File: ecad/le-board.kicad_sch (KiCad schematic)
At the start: 72 parts

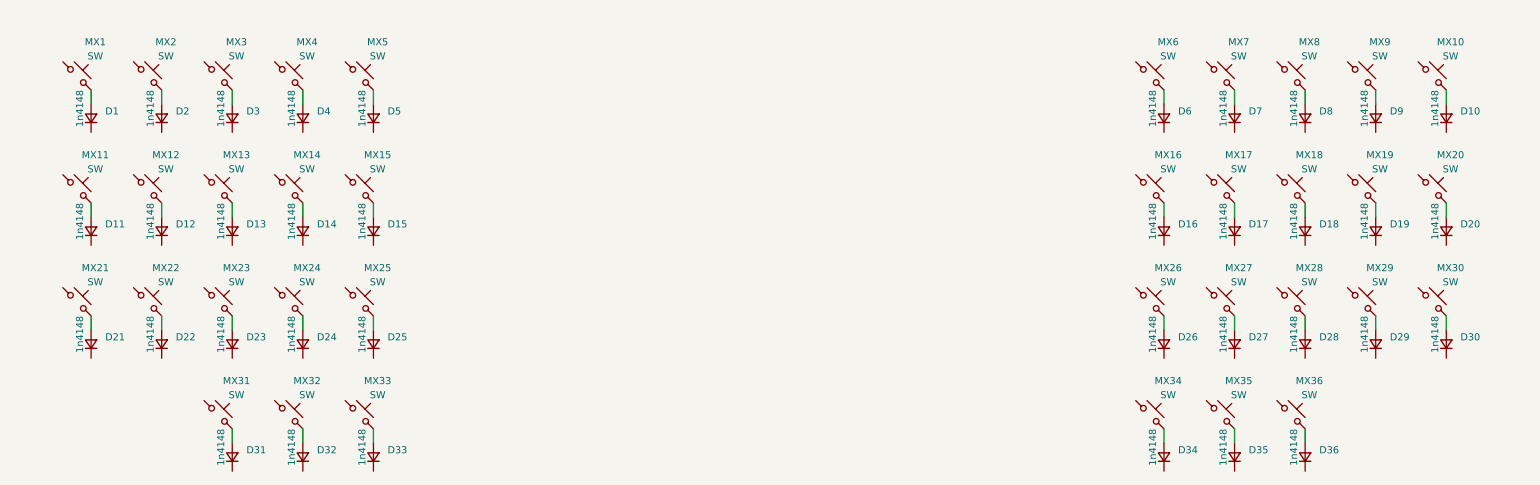
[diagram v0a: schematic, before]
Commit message: Added keyboard_pad_left, keyboard_pad_right. Added LDOs, Added USB C connector. Added initial placement for keys.
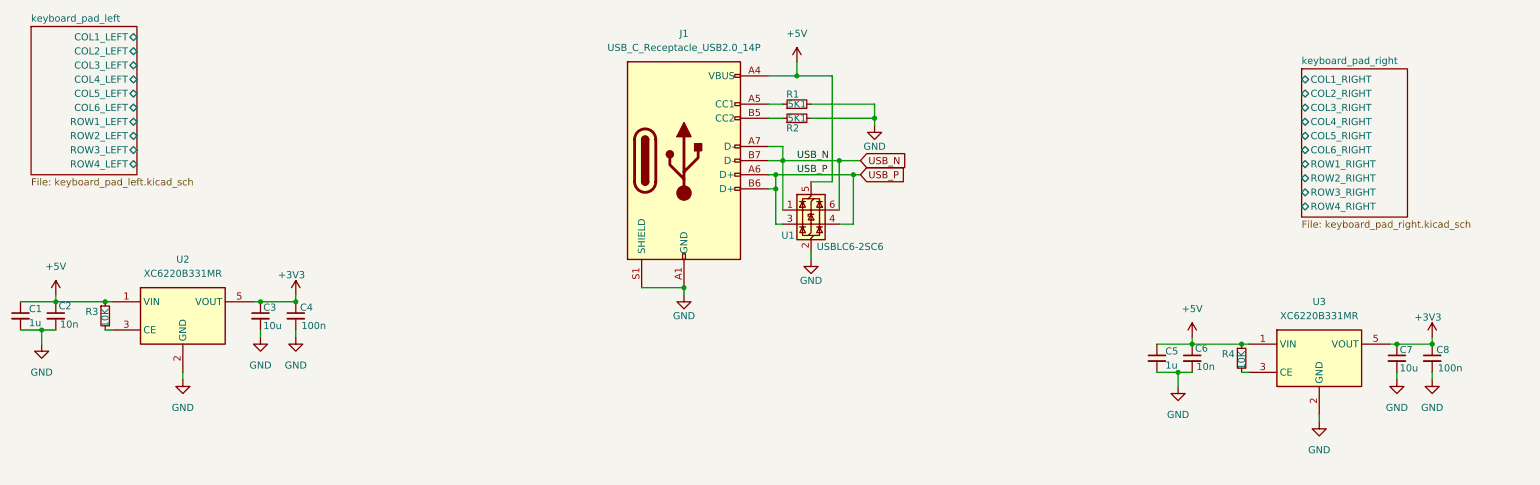
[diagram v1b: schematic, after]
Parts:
- removed D1, D10, D11, D12, D13, D14, D15, D16, D17, D18, D19, D2, D20, D21, D22, D23, D24, D25, D26, D27, D28, D29, D3, D30, D31, D32, D33, D34, D35, D36, D4, D5, D6, D7, D8, D9: 1n4148, Diode_SMD:D_SOD-123, symbol Device:D_Small
- removed MX1, MX10, MX11, MX12, MX13, MX14, MX15, MX16, MX17, MX18, MX19, MX2, MX20, MX21, MX22, MX23, MX24, MX25, MX26, MX27, MX28, MX29, MX3, MX30, MX31, MX32, MX33, MX34, MX35, MX36, MX4, MX5, MX6, MX7, MX8, MX9: SW, PCM_Switch_Keyboard_Cherry_MX:SW_Cherry_MX_PCB_1.00u, symbol PCM_marbastlib-mx:MX_SW_solder
- added C1, C5: 1u, Capacitor_SMD:C_0603_1608Metric, symbol Device:C_Small
- added C2, C6: 10n, Capacitor_SMD:C_0603_1608Metric, symbol Device:C_Small
- added C3, C7: 10u, Capacitor_SMD:C_0603_1608Metric, symbol Device:C_Small
- added C4, C8: 100n, Capacitor_SMD:C_0603_1608Metric, symbol Device:C_Small
- added J1: USB_C_Receptacle_USB2.0_14P, Connector_USB:USB_C_Receptacle_GCT_USB4105-xx-A_16P_TopMnt_Horizontal, symbol Connector:USB_C_Receptacle_USB2.0_14P
- added R1, R2: 5K1, Resistor_SMD:R_0402_1005Metric, symbol Device:R_Small
- added R3, R4: 10K, Resistor_SMD:R_0402_1005Metric, symbol Device:R_Small
- added U1: USBLC6-2SC6, Package_TO_SOT_SMD:SOT-23-6, symbol Power_Protection:USBLC6-2SC6
- added U2, U3: XC6220B331MR, Package_TO_SOT_SMD:SOT-23-5, symbol Regulator_Linear:XC6220B331MR
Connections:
- new net: J1.B5 (CC2), R2.1
- new net: R3.2, U2.3 (CE)
- new net: R4.2, U3.3 (CE)
- new net: J1.A5 (CC1), R1.1
- new net +3V3: C3.1, C4.1, C7.1, C8.1, U2.5 (VOUT), U3.5 (VOUT)
- new net +5V: C1.1, C2.1, C5.1, C6.1, J1.A4 (VBUS), J1.A9 (VBUS), J1.B4 (VBUS), J1.B9 (VBUS), R3.1, R4.1, U1.5 (VBUS), U2.1 (VIN), U3.1 (VIN)
- new net GND: C1.2, C2.2, C3.2, C4.2, C5.2, C6.2, C7.2, C8.2, J1.A1 (GND), J1.A12 (GND), J1.B1 (GND), J1.B12 (GND), J1.S1 (SHIELD), R1.2, R2.2, U1.2 (GND), U2.2 (GND), U3.2 (GND)
- new net USB_N: J1.A7 (D-), J1.B7 (D-), U1.1 (I/O1), U1.6 (I/O1)
- new net USB_P: J1.A6 (D+), J1.B6 (D+), U1.3 (I/O2), U1.4 (I/O2)
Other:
- added sheet keyboard_pad_left (keyboard_pad_left.kicad_sch)
- added sheet keyboard_pad_right (keyboard_pad_right.kicad_sch)

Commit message: Added 80% Schematic Finished.
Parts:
- added C10, C11, C21, C22: 100pF, symbol Device:C_Small
- added C12, C13, C19, C20: 1uF, symbol Device:C_Small
- added C14, C15, C16, C17, C24, C25, C27, C28: 12pF, symbol Device:C_Small
- added C18, C26: 1pF, symbol Device:C_Small
- added C23, C31, C32, C9: 100nF, symbol Device:C_Small
- added C29, C30: 10uF, symbol Device:C_Small
- added D45, D46, D47, D48: RED, LED_SMD:LED_0603_1608Metric, symbol Device:LED_Small_Filled
- added J2, J7: FL, Connector_Coaxial:U.FL_Hirose_U.FL-R-SMT-1_Vertical, symbol Connector:Conn_Coaxial
- added J3: FPC_LPAD, symbol Connector_Generic:Conn_01x10
- added J4: FPC_LMCU, symbol Connector_Generic:Conn_01x10
- added J5: FPC_RPAD, symbol Connector_Generic:Conn_01x10
- added J6: FPC_RMCU, symbol Connector_Generic:Conn_01x10
- added J8, J9: JST_S2B-PH-SM4-TB, ESP32-DevKit-101-footprint-lib:S2B-PH-SM4-TB, symbol ESP32-DevKit-101-symbol-lib:JST_S2B-PH-SM4-TB
- added L1, L5: 10uH, symbol Device:L_Small
- added L2, L4: 15uH, symbol Device:L_Small
- added L3, L6: 3.3nF, symbol Device:L_Small
- added Q1, Q2: FS8205A, ESP32-DevKit-101-footprint-lib:FS8205A_SOT23-6, symbol ESP32-DevKit-101-symbol-lib:FS8205A
- added R10, R12, R13, R5: 1K, symbol Device:R_Small
- added R11, R7: 10K, symbol Device:R_Small
- added R14, R9: 100R, symbol Device:R_Small
- added R15, R6: 1K2, symbol Device:R_Small
- added R16, R8: 2K, symbol Device:R_Small
- added U10, U6: MAX17048, Package_DFN_QFN:DFN-8-1EP_2x2mm_P0.5mm_EP0.7x1.3mm, symbol PCM_marbastlib-various:MAX17048
- added U11, U9: DW01, Package_TO_SOT_SMD:SOT-23-6, symbol ESP32-DevKit-101-symbol-lib:DW01
- added U4, U5: nRF52832-QFxx, Package_DFN_QFN:QFN-48-1EP_6x6mm_P0.4mm_EP4.6x4.6mm, symbol MCU_Nordic:nRF52832-QFxx
- added U7, U8: TP4056, Package_SO:SOIC-8-1EP_3.9x4.9mm_P1.27mm_EP2.29x3mm, symbol ESP32-DevKit-101-symbol-lib:TP4056-42-ESOP8
- added Y1, Y3: 32.768kHz, symbol Device:Crystal_Small
- added Y2, Y4: 32Mhz, symbol Device:Crystal_Small
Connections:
- net +5V: now also D45.2 (A), D46.2 (A), D47.2 (A), D48.2 (A), U7.4 (VCC), U7.8 (CE), U8.4 (VCC), U8.8 (CE)
- net GND: now also C10.2, C11.2, C12.2, C13.2, C14.2, C15.2, C16.2, C17.2, C18.2, C19.2, C20.2, C21.2, C22.2, C23.2, C24.2, C25.2, C26.2, C27.2, C28.2, C29.2, C30.2, C9.2, J2.2 (Ext), J7.2 (Ext), Q1.S1, Q2.S1, R15.2, R16.2, R6.2, R8.2, U10.1 (CTG), U10.4 (GND), U10.6 (QSTRT), U10.9 (GND), U4.31 (VSS), U4.45 (VSS), U4.49 (VSS), U5.31 (VSS), U5.45 (VSS), U5.49 (VSS), U6.1 (CTG), U6.4 (GND), U6.6 (QSTRT), U6.9 (GND), U7.1 (TEMP), U7.3 (GND), U7.9 (EP), U8.1 (TEMP), U8.3 (GND), U8.9 (EP)
- net keyboard_pad_left/COL1_LEFT: now also J3.1 (Pin_1)
- net keyboard_pad_left/COL2_LEFT: now also J3.2 (Pin_2)
- net keyboard_pad_left/COL3_LEFT: now also J3.3 (Pin_3)
- net keyboard_pad_left/COL4_LEFT: now also J3.4 (Pin_4)
- net keyboard_pad_left/COL5_LEFT: now also J3.5 (Pin_5)
- net keyboard_pad_left/COL6_LEFT: now also J3.6 (Pin_6)
- net keyboard_pad_left/ROW1_LEFT: now also J3.7 (Pin_7)
- net keyboard_pad_left/ROW2_LEFT: now also J3.8 (Pin_8)
- net keyboard_pad_left/ROW3_LEFT: now also J3.9 (Pin_9)
- net keyboard_pad_left/ROW4_LEFT: now also J3.10 (Pin_10)
- net keyboard_pad_right/COL1_RIGHT: now also J5.1 (Pin_1)
- net keyboard_pad_right/COL2_RIGHT: now also J5.2 (Pin_2)
- net keyboard_pad_right/COL3_RIGHT: now also J5.3 (Pin_3)
- net keyboard_pad_right/COL4_RIGHT: now also J5.4 (Pin_4)
- net keyboard_pad_right/COL5_RIGHT: now also J5.5 (Pin_5)
- net keyboard_pad_right/COL6_RIGHT: now also J5.6 (Pin_6)
- net keyboard_pad_right/ROW1_RIGHT: now also J5.7 (Pin_7)
- net keyboard_pad_right/ROW2_RIGHT: now also J5.8 (Pin_8)
- net keyboard_pad_right/ROW3_RIGHT: now also J5.9 (Pin_9)
- net keyboard_pad_right/ROW4_RIGHT: now also J5.10 (Pin_10)
- net +3V3 renamed VDD_nRF_L
- net VDD_nRF_L: now also C13.1, R7.1, U4.13 (VDD), U4.36 (VDD), U4.48 (VDD); no longer C7.1, C8.1, U3.5 (VOUT)
- new net: Q1.D1/D2, Q1.D1/D2
- new net: Q1.G2, U9.1 (OD)
- new net: C31.2, J8.2 (Pin_2), Q1.S2, U9.6 (GND)
- new net: D45.1 (K), R10.1
- new net: R8.1, U9.2 (CS)
- new net: L1.1, L2.2
- new net: L1.2, U4.47 (DCC)
- new net: C18.1, L3.2, U4.30 (ANT)
- new net: C16.1, U4.35 (XC2), Y2.2
- new net: C12.1, L2.1, U4.46 (DEC4)
- new net: R10.2, U8.6 (STDBY)
- new net: R6.1, U8.2 (PROG)
- new net: Q1.G1, U9.3 (OC)
- new net: C22.1, U5.32 (DEC2)
- new net: C24.1, U5.2 (P0.00/XL1), Y3.2
- new net: C32.1, R14.2, U11.5 (VCC)
- new net: C32.2, J9.2 (Pin_2), Q2.S2, U11.6 (GND)
- new net: C20.1, L4.1, U5.46 (DEC4)
- new net: L4.2, L5.1
- new net: C28.1, U5.35 (XC2), Y4.2
- new net: C23.1, U5.1 (DEC1)
- new net: Q2.G2, U11.1 (OD)
- new net: R16.1, U11.2 (CS)
- new net: Q2.G1, U11.3 (OC)
- new net: Q2.D1/D2, Q2.D1/D2
- new net: D48.1 (K), R13.1
- new net: R13.2, U7.7 (CHRG)
- new net: C21.1, U5.33 (DEC3)
- new net: J2.1 (In), L3.1
- new net: J7.1 (In), L6.1
- new net: C26.1, L6.2, U5.30 (ANT)
- new net: C27.1, U5.34 (XC1), Y4.1
- new net: C31.1, R9.2, U9.5 (VCC)
- new net: D47.1 (K), R12.1
- new net: R12.2, U7.6 (STDBY)
- new net: C25.1, U5.3 (P0.01/XL2), Y3.1
- new net: L5.2, U5.47 (DCC)
- new net: D46.1 (K), R5.1
- new net: C17.1, U4.34 (XC1), Y2.1
- new net: R5.2, U8.7 (CHRG)
- new net: C14.1, U4.2 (P0.00/XL1), Y1.2
- new net: C15.1, U4.3 (P0.01/XL2), Y1.1
- new net: C9.1, U4.1 (DEC1)
- new net: R15.1, U7.2 (PROG)
- new net: C10.1, U4.32 (DEC2)
- new net: C11.1, U4.33 (DEC3)
- new net +VBAT_L: C29.1, J8.1 (Pin_1), R9.1, U6.2 (CELL), U6.3 (VDD), U8.5 (BAT)
- new net +VBAT_R: C30.1, J9.1 (Pin_1), R14.1, U10.2 (CELL), U10.3 (VDD), U7.5 (BAT)
- new net ALRT_BAT_L: R11.2, R7.2, U10.5 (~{ALRT}), U6.5 (~{ALRT})
- new net P0.10_ROW3_LEFT: J4.9 (Pin_9), U4.12 (NFC2/P0.10)
- new net P0.10_ROW3_RIGHT: J6.9 (Pin_9), U5.12 (NFC2/P0.10)
- new net P0.11_ROW4_LEFT: J4.10 (Pin_10), U4.14 (P0.11)
- new net P0.11_ROW4_RIGHT: J6.10 (Pin_10), U5.14 (P0.11)
- new net P0.2_COL1_LEFT: J4.1 (Pin_1), U4.4 (P0.02/AIN0)
- new net P0.2_COL1_RIGHT: J6.1 (Pin_1), U5.4 (P0.02/AIN0)
- new net P0.3_COL2_LEFT: J4.2 (Pin_2), U4.5 (P0.03/AIN1)
- new net P0.3_COL2_RIGHT: J6.2 (Pin_2), U5.5 (P0.03/AIN1)
- new net P0.4_COL3_LEFT: J4.3 (Pin_3), U4.6 (P0.04/AIN2)
- new net P0.4_COL3_RIGHT: J6.3 (Pin_3), U5.6 (P0.04/AIN2)
- new net P0.5_COL4_LEFT: J4.4 (Pin_4), U4.7 (P0.05/AIN3)
- new net P0.5_COL4_RIGHT: J6.4 (Pin_4), U5.7 (P0.05/AIN3)
- new net P0.6_COL5_LEFT: J4.5 (Pin_5), U4.8 (P0.06)
- new net P0.6_COL5_RIGHT: J6.5 (Pin_5), U5.8 (P0.06)
- new net P0.7_COL6_LEFT: J4.6 (Pin_6), U4.9 (P0.07)
- new net P0.7_COL6_RIGHT: J6.6 (Pin_6), U5.9 (P0.07)
- new net P0.8_ROW1_LEFT: J4.7 (Pin_7), U4.10 (P0.08)
- new net P0.8_ROW1_RIGHT: J6.7 (Pin_7), U5.10 (P0.08)
- new net P0.9_ROW2_LEFT: J4.8 (Pin_8), U4.11 (NFC1/P0.09)
- new net P0.9_ROW2_RIGHT: J6.8 (Pin_8), U5.11 (NFC1/P0.09)
- new net RESET_L: U4.24 (P0.21/~{RESET})
- new net RESET_R: U5.24 (P0.21/~{RESET})
- new net SDA_L: U10.8 (SDA), U6.8 (SDA)
- new net SDA_R: U10.7 (SCL), U6.7 (SCL)
- new net SWDCLK_L: U4.25 (SWDCLK)
- new net SWDCLK_R: U5.25 (SWDCLK)
- new net SWDIO_L: U4.26 (SWDIO)
- new net SWDIO_R: U5.26 (SWDIO)
- new net VDD_nRF_R: C19.1, C7.1, C8.1, R11.1, U3.5 (VOUT), U5.13 (VDD), U5.36 (VDD), U5.48 (VDD)
- no-connect marks 0 -> 4
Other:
- note added: "Battery Charging Circuit"
- note added: "Battery Monitoring"
- note added: "DC/DC 5V -> 3V3"
- note added: "Main Oscillator"
- title: (none) -> Le Board
- moved on the sheet: C1, C2, C3, C4, C5, C6, C7, C8, J1, R1, R2, R3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

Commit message: Dodao sam pogo pinove za UART i za BAT(Napajanje za punjenje baterije), i Konektore za programiranje. Nazivi napajanja jos nisu sredjeni nabacano je, treba da se sredi gde sta ide ASAP.
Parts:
- added J10: POGO_UART_L, symbol Connector_Generic:Conn_01x03
- added J11: POGO_BAT_L, symbol Connector_Generic:Conn_01x02
- added J12: POGO_UART_R, symbol Connector_Generic:Conn_01x03
- added J13: POGO_BAT_R, symbol Connector_Generic:Conn_01x02
- added J14, J15: J-LINK_L, symbol Connector_Generic:Conn_02x03_Counter_Clockwise
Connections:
- net GND: now also J10.1 (Pin_1), J11.1 (Pin_1), J12.1 (Pin_1), J13.1 (Pin_1), J14.4 (Pin_4), J14.5 (Pin_5), J15.4 (Pin_4), J15.5 (Pin_5)
- net RESET_L: now also J14.6 (Pin_6)
- net RESET_R: now also J15.6 (Pin_6)
- net SWDCLK_L: now also J14.2 (Pin_2)
- net SWDCLK_R: now also J15.2 (Pin_2)
- net SWDIO_L: now also J14.3 (Pin_3)
- net SWDIO_R: now also J15.3 (Pin_3)
- new net BAT_L: J11.2 (Pin_2)
- new net BAT_R: J13.2 (Pin_2)
- new net UART_RX_L: J10.2 (Pin_2)
- new net UART_RX_R: J12.2 (Pin_2)
- new net UART_TX_L: J10.3 (Pin_3)
- new net UART_TX_R: J12.3 (Pin_3)
- new net VBUS: J14.1 (Pin_1), J15.1 (Pin_1)
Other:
- note added: "POGO INTERFACE"
